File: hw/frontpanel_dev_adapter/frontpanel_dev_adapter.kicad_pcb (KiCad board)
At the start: 4 copper layers, 100 x 100 mm, 122 parts, among them J201 KLD-0202-A, J202 Conn_WR-FAST_01x04, J203 Molex_MicroFit_30-43045-0421, J301 FFC_conn_14p, J302 FFC_conn_14p, J303 JST_S2B-PH-SM4-TB, J501 Conn_01x20, J502 Conn_01x20, J503 SWD, J504 STX-3501-3N_(TTL-232R-xV-AJ), J601 Conn_02x32_Odd_Even, J602 Conn_02x32_Odd_Even, J603 Conn_02x32_Odd_Even, J604 Conn_02x32_Odd_Even, M301 FFC_retention_clamp, M302 FFC_retention_clamp, M401 Fan_4pin, Q201 Si4497DY, Q301 DMG1012T, Q401 DMG1012T, Q501 AO3401A, SW501 SKHUxxE010, U201 TPS54332DDA, U202 TLV1117LV30DCY, U203 TLV1117LV30DCY, U301 TLV9051SIDBV, U401 74LVC2G17gw, U501 STM32F103CBTx, U502 W25Q64FV, U503 CAT24C256, U504 DS3231MZ, Y501 8.0M

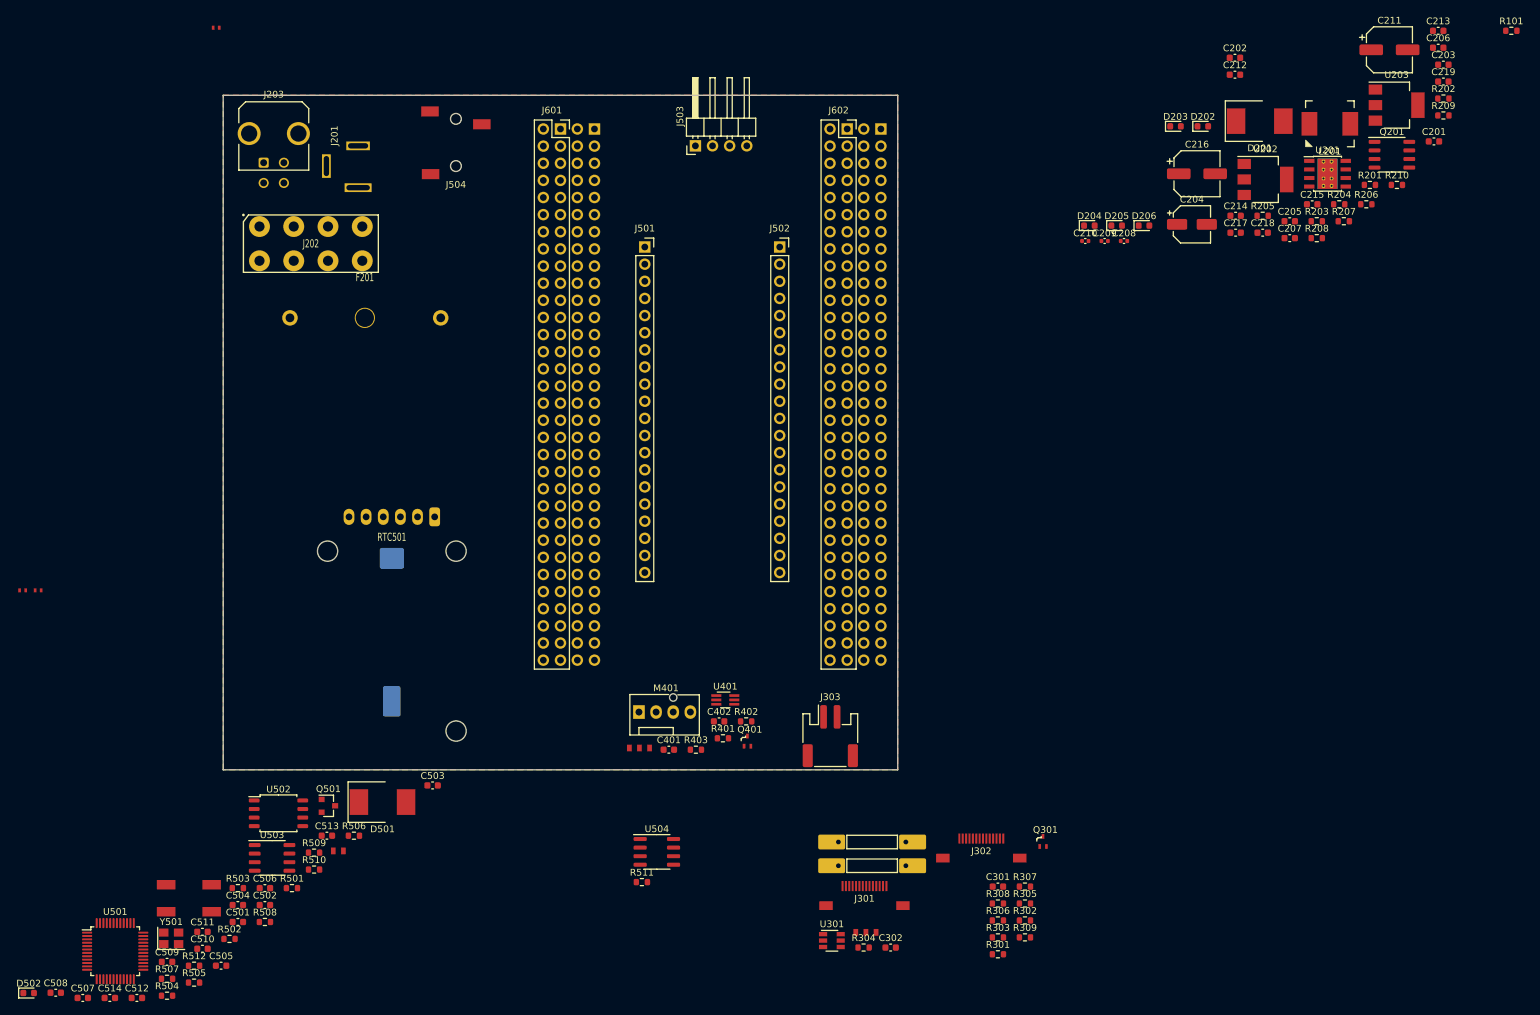
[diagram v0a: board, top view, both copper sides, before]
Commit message: Frontpanel adapter: PCB placement done incl logo, mounting holes. Some silk notations."
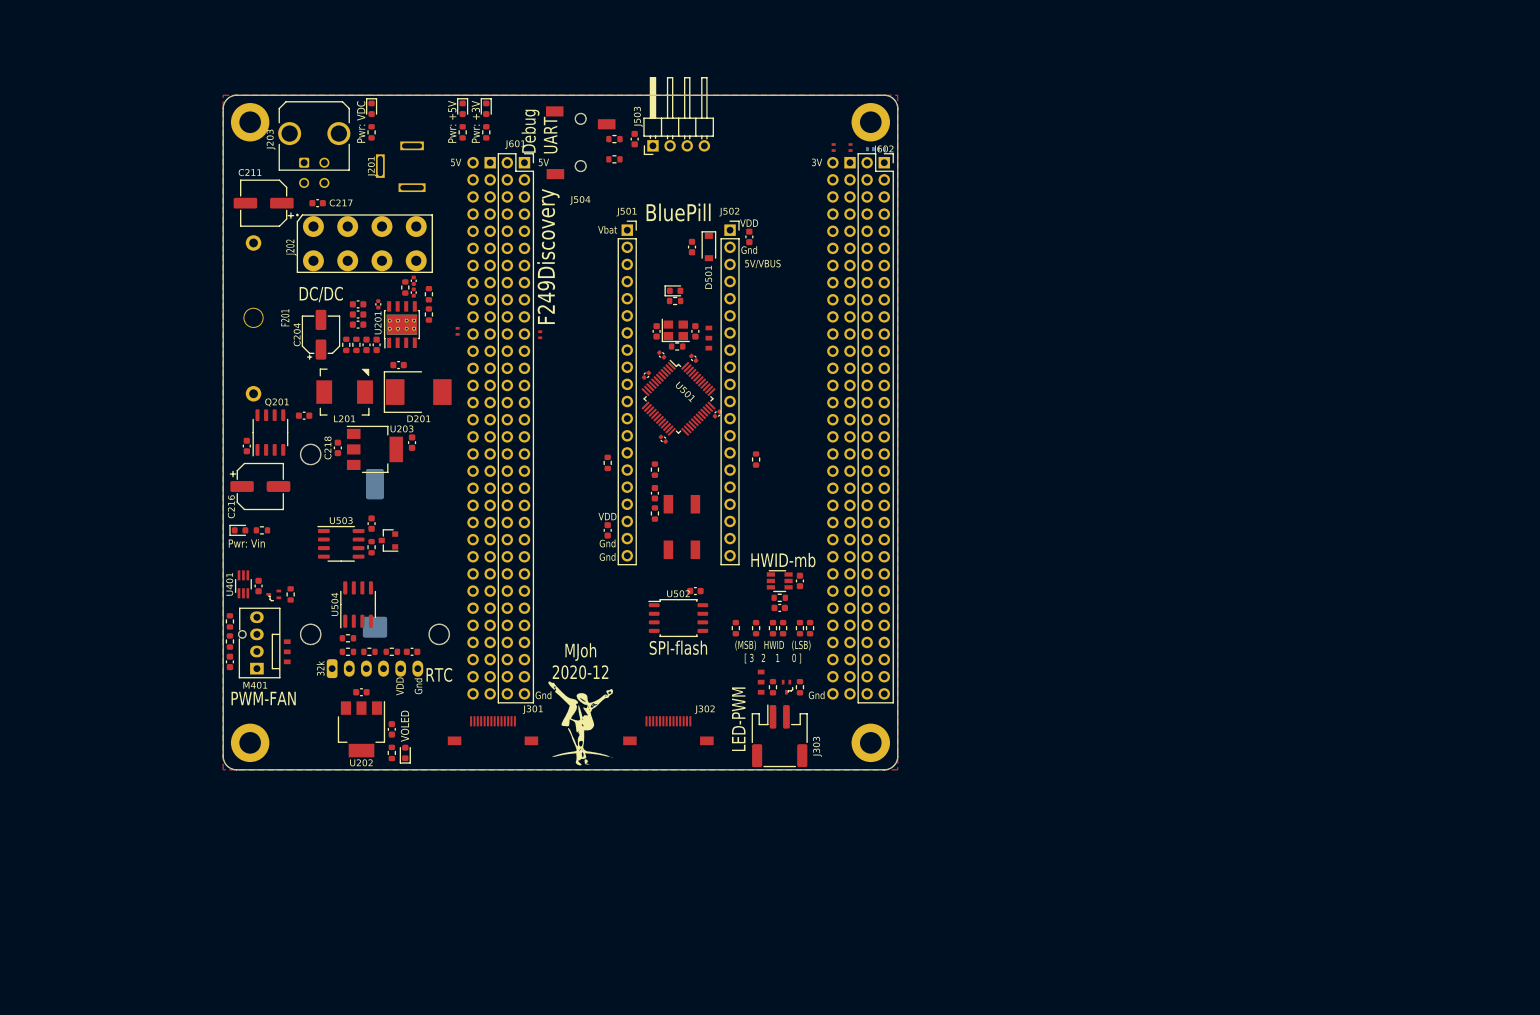
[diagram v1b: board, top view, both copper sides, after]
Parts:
- removed M301, M302: FFC_retention_clamp, customlib_mj_fp:FFC_retention_clamp_14pin_7_5mm
- added C515: 0.1u, Capacitor_SMD:C_0402_1005Metric, F.Cu at (119.8, 89.0)
- added H101: MountingHole_Pad, MountingHole:MountingHole_3.2mm_M3_ISO7380_Pad, F.Cu at (54.0, 54.0)
- added H102: MountingHole_Pad, MountingHole:MountingHole_3.2mm_M3_ISO7380_Pad, F.Cu at (146.0, 54.0)
- added H103: MountingHole_Pad, MountingHole:MountingHole_3.2mm_M3_ISO7380_Pad, F.Cu at (54.0, 146.0)
- added H104: MountingHole_Pad, MountingHole:MountingHole_3.2mm_M3_ISO7380_Pad, F.Cu at (146.0, 146.0)
- added JP604: dogbone_2_ud, customlib_mj_fp:db2_ud_0402, F.Cu at (143.0, 57.8)
- added JP605: dogbone_2_ud, customlib_mj_fp:db2_ud_0402, F.Cu at (140.5, 57.8)
- added JP606: dogbone_2_ud, customlib_mj_fp:db2_ud_0402, F.Cu at (84.8, 85.0)
- added Logo101: Logo_MJ, customlib_mj_fp:MJ_10.3x12.7, F.Cu at (103.0, 143.0)
- added REF**: Polarity_Center_Positive_6mm_SilkScreen, Symbol:Polarity_Center_Positive_6mm_SilkScreen, B.Cu at (81.5, 54.0)
- C501, C502, C503, C504: footprint Capacitor_SMD:C_0603_1608Metric -> Capacitor_SMD:C_0402_1005Metric
- D501: value MBRS340T3G -> B5819W; footprint customlib_mj_fp:MBRS3xx_SMC_CASE_403AC -> Diode_SMD:D_SOD-123
- JP501: footprint customlib_mj_fp:db2_ud_0603 -> customlib_mj_fp:db3_ud_0603
- JP601, JP602: moved to B.Cu
- moved C213 186.5 mm to (75.0, 144.0), turned to 90 degrees
- moved Q201 171.3 mm to (57.0, 100.0), turned to 90 degrees
- moved R210 171.1 mm to (75.0, 147.5), turned to 270 degrees
- moved C211 168.4 mm to (56.0, 66.0), turned to 180 degrees
- moved R207 166.8 mm to (55.8, 114.5), turned to 180 degrees
- moved C203 164.9 mm to (71.2, 87.0), turned to 90 degrees
- moved C206 164.9 mm to (70.0, 82.5)
- moved C219 162.0 mm to (78.0, 101.5), turned to 90 degrees
- moved U203 159.8 mm to (72.5, 102.5)
- moved C212 158.6 mm to (70.5, 138.5)
- moved C201 157.0 mm to (76.0, 90.0), turned to 180 degrees
- moved U202 156.9 mm to (70.5, 144.0), turned to 270 degrees
- moved R201 153.6 mm to (68.2, 87.0), turned to 90 degrees
- moved R202 153.2 mm to (80.5, 79.5), turned to 270 degrees
- moved C215 152.7 mm to (62.0, 97.5)
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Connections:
- R504 pad 1: GND -> Net-(R504-Pad1)
- U501 pad 20: GND -> Net-(R504-Pad1)
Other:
- outline, holes or cut-outs redrawn
- board text added: "(MSB) HWID (LSB) [ 3 2 1 0 ]"
- board text added: "32k"
- board text added: "3V"
- board text added: "5V"
- board text added: "5V/VBUS"
- board text added: "BluePill"
- board text added: "DC/DC"
- board text added: "Debug UART"
- board text added: "F249Discovery"
- board text added: "Frontpanel FFC to MCU adapter"
- board text added: "Gnd"
- board text added: "HWID-mb"
- board text added: "LED-PWM"
- board text added: "MJoh 2020-12"
- board text added: "PWM-FAN"
- board text added: "Pwr: +3V"
- board text added: "Pwr: +5V"
- board text added: "Pwr: VDC"
- board text added: "Pwr: Vin"
- board text added: "RTC"
- board text added: "SPI-flash"
- board text added: "VDD"
- board text added: "VOLED"
- board text added: "Vbat"
- board text added: "ca 7-14V"

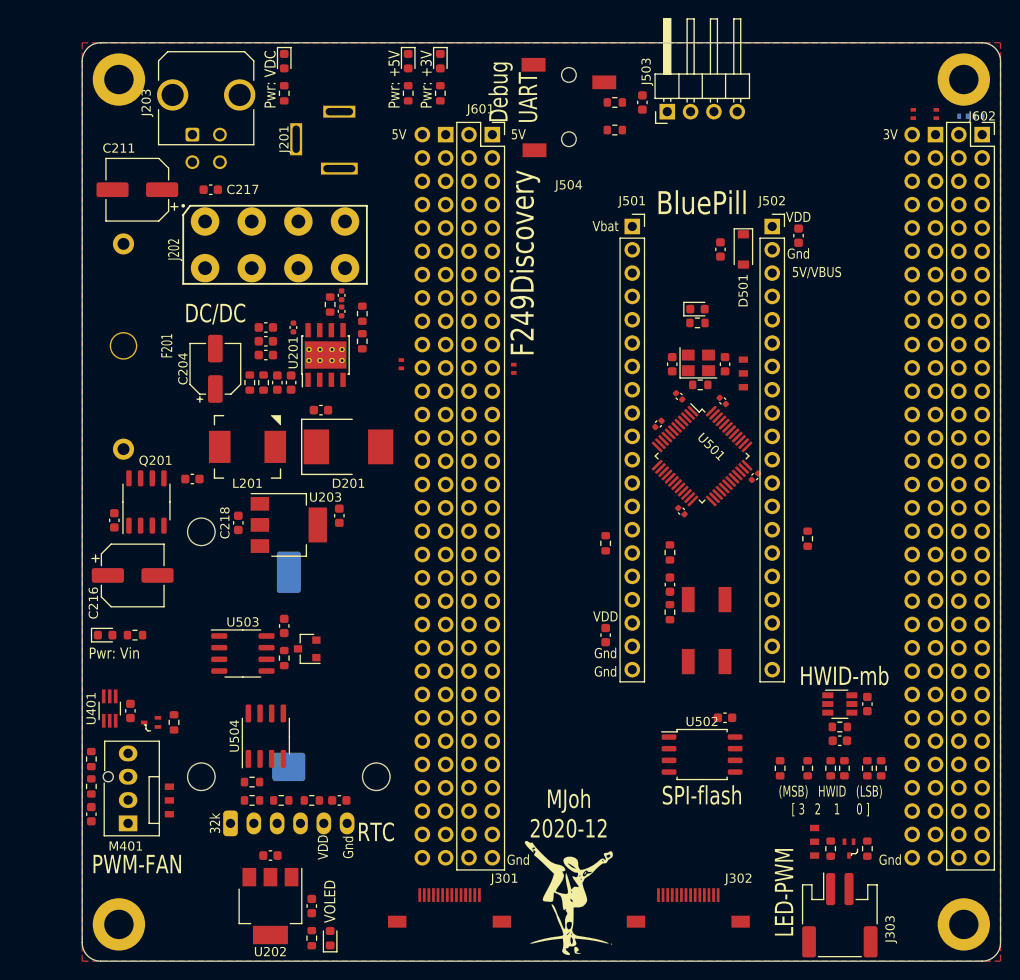
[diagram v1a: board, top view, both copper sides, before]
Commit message: FP adapter/devboard: some initial routing
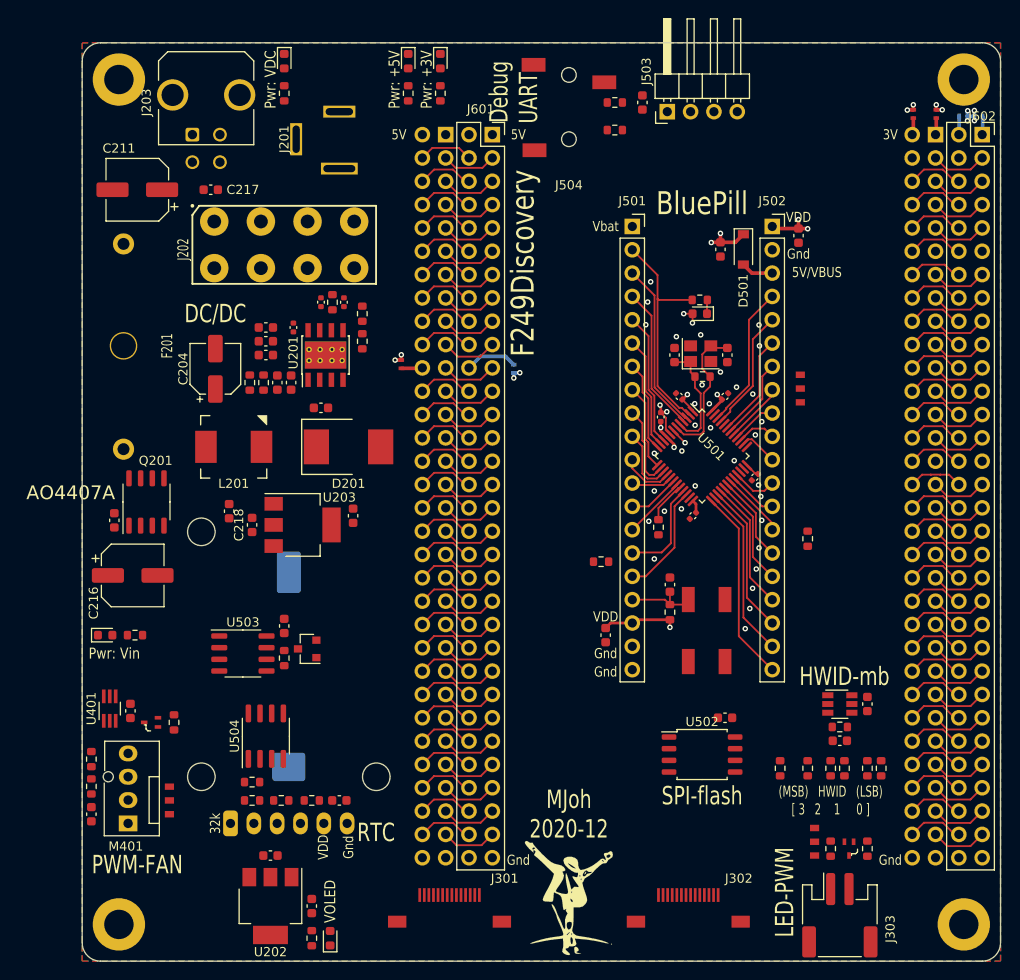
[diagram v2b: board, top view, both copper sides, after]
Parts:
- JP603: moved to B.Cu
- moved JP501 6.42 mm to (128.2, 87.7)
- moved C215 5.32 mm to (66.0, 101.0), turned to 270 degrees
- moved R504 3.02 mm to (112.8, 102.8)
- moved R505 2.51 mm to (117.2, 78.0), turned to 0 degrees
- moved C210 2.37 mm to (76.0, 78.2)
- moved R101 2.06 mm to (106.5, 106.5), turned to 0 degrees
- moved C218 1.52 mm to (68.5, 102.5)
- moved C219 1.50 mm to (79.5, 101.5)
- moved L201 1.50 mm to (66.5, 94.0)
- moved U203 1.50 mm to (74.0, 102.5)
- moved C503 1.35 mm to (116.5, 101.5), turned to 225 degrees
- moved C209 1.03 mm to (78.5, 78.2)
- moved C506 1.03 mm to (114.5, 84.0)
- moved C508 1.03 mm to (120.2, 84.0)
- moved Y501 1.03 mm to (117.3, 83.8)
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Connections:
- J603 pad 22: VDD -> Net-(J603-Pad22)
- J604 pad 1: VDD -> Net-(J604-Pad1)
- J604 pad 2: VDD -> Net-(J604-Pad2)
- JP604 pad 2: VDD -> Net-(J604-Pad1)
- JP605 pad 1: VDD -> Net-(J604-Pad2)
- JP606 pad 1: VDD -> Net-(J603-Pad22)
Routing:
- net VDD: track 0.00 -> 34.5 mm, vias 0 -> 21
- net AUX_BOOT0: track 0.00 -> 30.7 mm
- net ~SYS_RSTn~: track 0.00 -> 27.3 mm
- net ~FP_BTN_2An~: track 0.00 -> 24.9 mm
- net 32k: track 0.00 -> 24.4 mm
- net ~FP_BTN_2Bn~: track 0.00 -> 22.6 mm
- net I2C1_SDA: track 0.00 -> 21.8 mm
- net FAN1_RPM: track 0.00 -> 20.7 mm
- net ~FP_ENC_SWn~: track 0.00 -> 20.2 mm
- net I2C1_SCL: track 0.00 -> 19.4 mm
- net /F429Discovery connection/AUXUART7_RX: track 0.00 -> 18.4 mm
- net ~RTC_INTn~_SQW: track 0.00 -> 18.3 mm
- net ~DISP_CSn~: track 0.00 -> 17.9 mm
- net FP_ENC_B: track 0.00 -> 17.3 mm
- net ~AUX_INTn~: track 0.00 -> 16.0 mm
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- added copper zone on F.Cu, net GND
- added copper zone on In2.Cu, net GND
- added copper zone on In1.Cu, net VDD
- added copper zone on B.Cu, net VMAIN
- removed copper zone on In1.Cu, net GND
- removed copper zone on F.Cu, net VDD
- removed copper zone on In2.Cu, net VMAIN
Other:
- board text added: "AO4407A"
